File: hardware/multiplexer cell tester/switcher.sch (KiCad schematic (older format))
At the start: 29 parts, among them J3 Conn_01x10_Female, J4 Conn_01x10_Female, J5 A2 Select, J6 A1 Select, J7 A0 Select, U10 ADG839YKSZ-REEL7, U11 ADG839YKSZ-REEL7, U12 ADG839YKSZ-REEL7, U2 CD4518BM96, U2 SN74LVC1G14DRL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

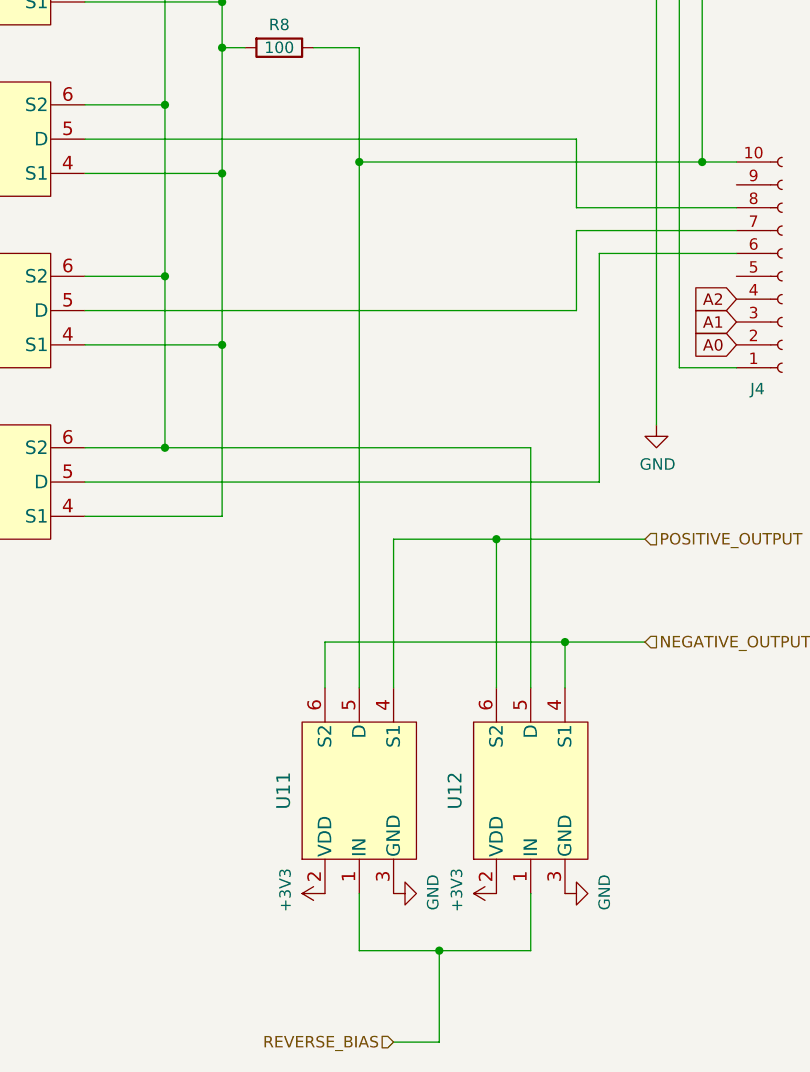
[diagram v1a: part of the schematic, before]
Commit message: Create holders
- Created holders for the payload
- Sliced holders for testing
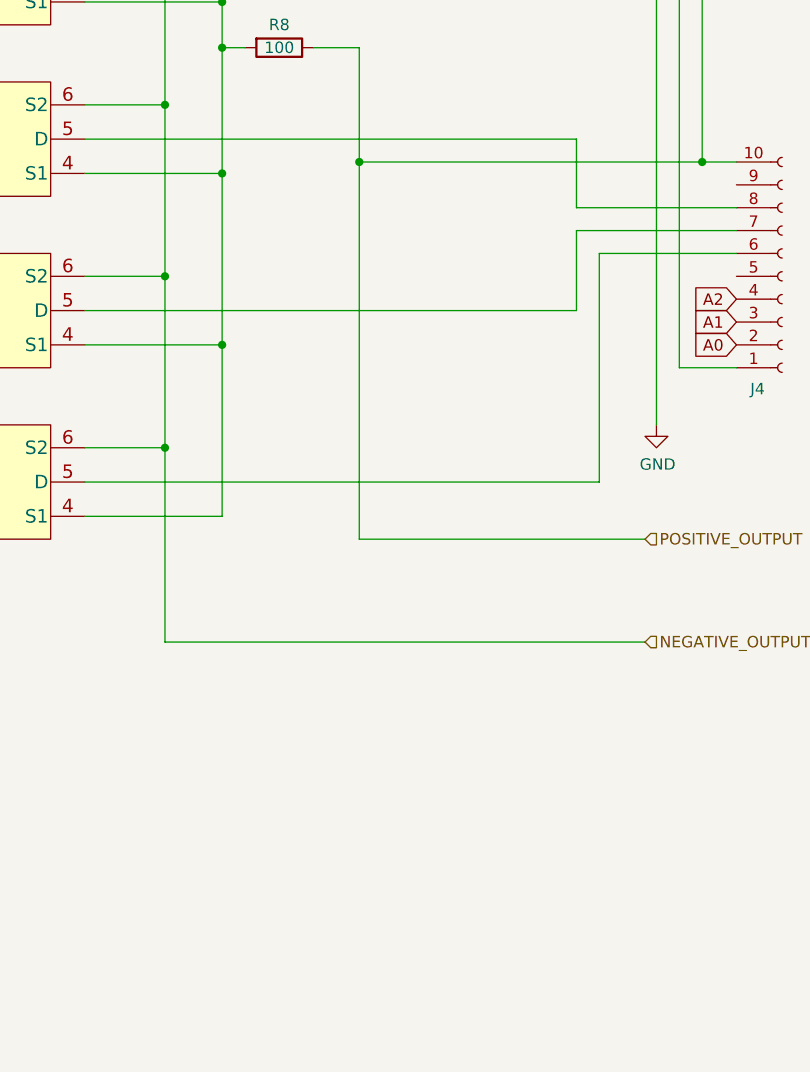
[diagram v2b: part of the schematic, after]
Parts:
- removed U11, U12: ADG839YKSZ-REEL7, ul_ADG839YKSZ-REEL7:ADG839YKSZ-REEL7, symbol ADG839:ADG839YKSZ-REEL7
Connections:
- net NEGATIVE_OUTPUT: now also U10.6 (S2), U5.6 (S2), U6.6 (S2), U7.6 (S2), U8.6 (S2), U9.6 (S2)
- net POSITIVE_OUTPUT: now also J3.1 (Pin_1), J4.10 (Pin_10), R5.1
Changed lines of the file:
@@
 Connection ~ 10050 5750
-Wire Wire Line
-	10050 5750 10050 6500
 Wire Wire Line
 	9700 6500 10050 6500
@@
 Wire Wire Line
 	10700 4750 10900 4750
-$Comp
-L ADG839:ADG839YKSZ-REEL7 U11
-U 1 1 64930E1A
-P 10900 8000
-F 0 "U11" H 10900 8331 60  0000 C CNN
-F 1 "ADG839YKSZ-REEL7" H 10900 8331 60  0001 C CNN
-F 2 "ul_ADG839YKSZ-REEL7:ADG839YKSZ-REEL7" H 10900 8290 60  0001 C CNN
-F 3 "" H 10450 8000 60  0000 C CNN
-	1    10900 8000
-	0    -1   -1   0
-$EndComp
-Wire Wire Line
-	10750 7350 10750 7550
-Wire Wire Line
-	11800 7550 11800 7350
-Wire Wire Line
-	11050 6900 11050 7550
-Wire Wire Line
-	11500 6900 11500 7550
-$Comp
-L power:+3V3 #PWR?
-U 1 1 64B73EC4
-P 10750 8450
-AR Path="/6313FC31/64B73EC4" Ref="#PWR?"  Part="1"
-AR Path="/64B73EC4" Ref="#PWR0210"  Part="1"
-AR Path="/648F7944/64B73EC4" Ref="#PWR0155"  Part="1"
-F 0 "#PWR0155" H 10750 8300 50  0001 C CNN
-F 1 "+3V3" H 10765 8623 50  0000 C CNN
-F 2 "" H 10750 8450 50  0001 C CNN
-F 3 "" H 10750 8450 50  0001 C CNN
-	1    10750 8450
-	0    -1   -1   0
-$EndComp
-$Comp
-L power:+3V3 #PWR?
-U 1 1 64B74C45
-P 11500 8450
-AR Path="/6313FC31/64B74C45" Ref="#PWR?"  Part="1"
-AR Path="/64B74C45" Ref="#PWR0211"  Part="1"
-AR Path="/648F7944/64B74C45" Ref="#PWR0156"  Part="1"
-F 0 "#PWR0156" H 11500 8300 50  0001 C CNN
-F 1 "+3V3" H 11515 8623 50  0000 C CNN
-F 2 "" H 11500 8450 50  0001 C CNN
-F 3 "" H 11500 8450 50  0001 C CNN
-	1    11500 8450
-	0    -1   -1   0
-$EndComp
-$Comp
-L power:GND #PWR?
-U 1 1 64B75863
-P 11050 8450
-AR Path="/6313FC31/64B75863" Ref="#PWR?"  Part="1"
-AR Path="/64B75863" Ref="#PWR0212"  Part="1"
-AR Path="/648F7944/64B75863" Ref="#PWR0157"  Part="1"
-F 0 "#PWR0157" H 11050 8200 50  0001 C CNN
-F 1 "GND" H 11055 8277 50  0000 C CNN
-F 2 "" H 11050 8450 50  0001 C CNN
-F 3 "" H 11050 8450 50  0001 C CNN
-	1    11050 8450
-	0    -1   -1   0
-$EndComp
-$Comp
-L power:GND #PWR?
-U 1 1 64B74F6E
-P 11800 8450
-AR Path="/6313FC31/64B74F6E" Ref="#PWR?"  Part="1"
-AR Path="/64B74F6E" Ref="#PWR0213"  Part="1"
-AR Path="/648F7944/64B74F6E" Ref="#PWR0158"  Part="1"
-F 0 "#PWR0158" H 11800 8200 50  0001 C CNN
-F 1 "GND" H 11805 8277 50  0000 C CNN
-F 2 "" H 11800 8450 50  0001 C CNN
-F 3 "" H 11800 8450 50  0001 C CNN
-	1    11800 8450
-	0    -1   -1   0
-$EndComp
-$Comp
-L ADG839:ADG839YKSZ-REEL7 U12
-U 1 1 6496588F
-P 11650 8000
-F 0 "U12" H 11650 8331 60  0000 C CNN
-F 1 "ADG839YKSZ-REEL7" H 11650 8331 60  0001 C CNN
-F 2 "ul_ADG839YKSZ-REEL7:ADG839YKSZ-REEL7" H 11650 8290 60  0001 C CNN
-F 3 "" H 11200 8000 60  0000 C CNN
-	1    11650 8000
-	0    -1   -1   0
-$EndComp
-Wire Wire Line
-	10750 7350 11800 7350
-Wire Wire Line
-	11050 6900 11500 6900
-Wire Wire Line
-	10900 8450 10900 8700
-Wire Wire Line
-	10900 8700 11250 8700
-Wire Wire Line
-	11650 8700 11650 8450
-Wire Wire Line
-	11250 8700 11250 9100
-Wire Wire Line
-	11250 9100 11050 9100
-Connection ~ 11250 8700
-Wire Wire Line
-	11250 8700 11650 8700
-Wire Wire Line
-	11650 7550 11650 6500
-Wire Wire Line
-	10050 6500 11650 6500
-Wire Wire Line
-	10900 7550 10900 5250
 Wire Wire Line
 	12400 4200 12400 5250
@@
 Text HLabel 12150 7350 2    50   Input ~ 0
 NEGATIVE_OUTPUT
-Wire Wire Line
-	12150 6900 11500 6900
-Connection ~ 11500 6900
-Wire Wire Line
-	11800 7350 12150 7350
-Connection ~ 11800 7350
 $Comp
 L 74xGxx:SN74LVC1G14DRL U2
@@
 Wire Wire Line
 	5700 4550 5800 4550
-Text HLabel 11050 9100 0    50   Input ~ 0
-REVERSE_BIAS
 Text HLabel 12100 4000 0    50   Input ~ 0
 SDA
@@
 	12400 5250 10900 5250
 Connection ~ 12400 5250
+Wire Wire Line
+	10900 5250 10900 4750
+Wire Wire Line
+	10050 5750 10050 6500
+Wire Wire Line
+	10900 6900 10900 5250
+Wire Wire Line
+	10900 6900 12150 6900
 Connection ~ 10900 5250
 Wire Wire Line
-	10900 5250 10900 4750
+	10050 7350 10050 6500
+Wire Wire Line
+	10050 7350 12150 7350
 $EndSCHEMATC

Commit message: Finalized curve tracer
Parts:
- removed C18, C20: 0.1u, Capacitor_SMD:C_0603_1608Metric, symbol Device:C
- added R27, R29, R30, R31, R32: 400, Resistor_SMD:R_0603_1608Metric, symbol Device:R
- R5: value 100 -> 400
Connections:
- net POSITIVE_OUTPUT: now also R27.1, R29.1, R30.1, R31.1, R32.1
- new net: R32.2, U10.4 (S1)
- new net: R5.2, U7.4 (S1)
- new net: R30.2, U8.4 (S1)
- new net: R29.2, U6.4 (S1)
- new net: R31.2, U9.4 (S1)
- new net: R27.2, U5.4 (S1)
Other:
- moved on the sheet: C13, R8
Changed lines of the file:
@@
 Sheet 2 4
 Title "Perovskite Switching Circuit"
-Date "2023-07-08"
+Date "2023-09-08"
 Rev "B"
 Comp "Aerospace eXperimental Payloads | UNL Aerospace Club"
@@
 $EndComp
 $Comp
-L Device:C C?
-U 1 1 63AAB0E4
-P 3800 1250
-AR Path="/6313FC31/63AAB0E4" Ref="C?"  Part="1"
-AR Path="/63AAB0E4" Ref="C20"  Part="1"
-AR Path="/648F7944/63AAB0E4" Ref="C8"  Part="1"
-F 0 "C8" V 4052 1250 50  0000 C CNN
-F 1 "0.1u" V 3961 1250 50  0000 C CNN
-F 2 "Capacitor_SMD:C_0603_1608Metric" H 3838 1100 50  0001 C CNN
-F 3 "~" H 3800 1250 50  0001 C CNN
-	1    3800 1250
-	1    0    0    -1
-$EndComp
-$Comp
-L power:+3V3 #PWR?
-U 1 1 63AAB0EA
-P 3800 1100
-AR Path="/6313FC31/63AAB0EA" Ref="#PWR?"  Part="1"
-AR Path="/63AAB0EA" Ref="#PWR0172"  Part="1"
-AR Path="/648F7944/63AAB0EA" Ref="#PWR0131"  Part="1"
-F 0 "#PWR0131" H 3800 950 50  0001 C CNN
-F 1 "+3V3" H 3815 1273 50  0000 C CNN
-F 2 "" H 3800 1100 50  0001 C CNN
-F 3 "" H 3800 1100 50  0001 C CNN
-	1    3800 1100
-	1    0    0    -1
-$EndComp
-$Comp
-L power:GND #PWR?
-U 1 1 63AAB0F0
-P 3800 1400
-AR Path="/6313FC31/63AAB0F0" Ref="#PWR?"  Part="1"
-AR Path="/63AAB0F0" Ref="#PWR0173"  Part="1"
-AR Path="/648F7944/63AAB0F0" Ref="#PWR0132"  Part="1"
-F 0 "#PWR0132" H 3800 1150 50  0001 C CNN
-F 1 "GND" H 3805 1227 50  0000 C CNN
-F 2 "" H 3800 1400 50  0001 C CNN
-F 3 "" H 3800 1400 50  0001 C CNN
-	1    3800 1400
-	1    0    0    -1
-$EndComp
-$Comp
-L Device:C C?
-U 1 1 63AAB0F6
-P 3400 1250
-AR Path="/6313FC31/63AAB0F6" Ref="C?"  Part="1"
-AR Path="/63AAB0F6" Ref="C18"  Part="1"
-AR Path="/648F7944/63AAB0F6" Ref="C7"  Part="1"
-F 0 "C7" V 3652 1250 50  0000 C CNN
-F 1 "0.1u" V 3561 1250 50  0000 C CNN
-F 2 "Capacitor_SMD:C_0603_1608Metric" H 3438 1100 50  0001 C CNN
-F 3 "~" H 3400 1250 50  0001 C CNN
-	1    3400 1250
-	1    0    0    -1
-$EndComp
-$Comp
-L power:+3V3 #PWR?
-U 1 1 63AAB0FC
-P 3400 1100
-AR Path="/6313FC31/63AAB0FC" Ref="#PWR?"  Part="1"
-AR Path="/63AAB0FC" Ref="#PWR0174"  Part="1"
-AR Path="/648F7944/63AAB0FC" Ref="#PWR0133"  Part="1"
-F 0 "#PWR0133" H 3400 950 50  0001 C CNN
-F 1 "+3V3" H 3415 1273 50  0000 C CNN
-F 2 "" H 3400 1100 50  0001 C CNN
-F 3 "" H 3400 1100 50  0001 C CNN
-	1    3400 1100
-	1    0    0    -1
-$EndComp
-$Comp
-L power:GND #PWR?
-U 1 1 63AAB102
-P 3400 1400
-AR Path="/6313FC31/63AAB102" Ref="#PWR?"  Part="1"
-AR Path="/63AAB102" Ref="#PWR0175"  Part="1"
-AR Path="/648F7944/63AAB102" Ref="#PWR0134"  Part="1"
-F 0 "#PWR0134" H 3400 1150 50  0001 C CNN
-F 1 "GND" H 3405 1227 50  0000 C CNN
-F 2 "" H 3400 1400 50  0001 C CNN
-F 3 "" H 3400 1400 50  0001 C CNN
-	1    3400 1400
-	1    0    0    -1
-$EndComp
-$Comp
 L ADG839:ADG839YKSZ-REEL7 U10
 U 1 1 63F8A2FD
@@
 Wire Wire Line
 	10050 2750 10050 3500
-Wire Wire Line
-	10300 3050 9700 3050
 $Comp
 L Device:R R?
 U 1 1 6435678E
-P 10550 4750
+P 10550 4550
 AR Path="/6313FC31/6435678E" Ref="R?"  Part="1"
 AR Path="/6435678E" Ref="R5"  Part="1"
 AR Path="/648F7944/6435678E" Ref="R8"  Part="1"
-F 0 "R8" V 10450 4750 50  0000 C CNN
-F 1 "100" V 10550 4750 50  0000 C CNN
-F 2 "Resistor_SMD:R_0603_1608Metric" V 10480 4750 50  0001 C CNN
-F 3 "~" H 10550 4750 50  0001 C CNN
-	1    10550 4750
+F 0 "R8" V 10450 4550 50  0000 C CNN
+F 1 "400" V 10550 4550 50  0000 C CNN
+F 2 "Resistor_SMD:R_0603_1608Metric" V 10480 4550 50  0001 C CNN
+F 3 "~" H 10550 4550 50  0001 C CNN
+	1    10550 4550
 	0    1    1    0
 $EndComp
@@
 Wire Wire Line
 	9700 6500 10050 6500
-Wire Wire Line
-	10300 3050 10300 3800
-Wire Wire Line
-	9700 6800 10300 6800
-Wire Wire Line
-	9700 6050 10300 6050
-Connection ~ 10300 6050
-Wire Wire Line
-	9700 5300 10300 5300
-Connection ~ 10300 5300
-Wire Wire Line
-	10300 5300 10300 6050
-Wire Wire Line
-	9700 4550 10300 4550
-Connection ~ 10300 4550
-Wire Wire Line
-	9700 3800 10300 3800
-Connection ~ 10300 3800
-Wire Wire Line
-	10300 3800 10300 4550
-Wire Wire Line
-	10300 6050 10300 6800
 $Comp
 L ADG839:ADG839YKSZ-REEL7 U9
@@
 L Device:C C?
 U 1 1 64C38237
-P 5000 1250
+P 4650 1250
 AR Path="/6313FC31/64C38237" Ref="C?"  Part="1"
 AR Path="/64C38237" Ref="C25"  Part="1"
 AR Path="/648F7944/64C38237" Ref="C13"  Part="1"
-F 0 "C13" V 5252 1250 50  0000 C CNN
-F 1 "0.1u" V 5161 1250 50  0000 C CNN
-F 2 "Capacitor_SMD:C_0603_1608Metric" H 5038 1100 50  0001 C CNN
-F 3 "~" H 5000 1250 50  0001 C CNN
-	1    5000 1250
+F 0 "C13" V 4902 1250 50  0000 C CNN
+F 1 "0.1u" V 4811 1250 50  0000 C CNN
+F 2 "Capacitor_SMD:C_0603_1608Metric" H 4688 1100 50  0001 C CNN
+F 3 "~" H 4650 1250 50  0001 C CNN
+	1    4650 1250
 	1    0    0    -1
 $EndComp
@@
 L power:+3V3 #PWR?
 U 1 1 64C3823D
-P 5000 1100
+P 4650 1100
 AR Path="/6313FC31/64C3823D" Ref="#PWR?"  Part="1"
 AR Path="/64C3823D" Ref="#PWR0214"  Part="1"
 AR Path="/648F7944/64C3823D" Ref="#PWR0149"  Part="1"
-F 0 "#PWR0149" H 5000 950 50  0001 C CNN
-F 1 "+3V3" H 5015 1273 50  0000 C CNN
-F 2 "" H 5000 1100 50  0001 C CNN
-F 3 "" H 5000 1100 50  0001 C CNN
-	1    5000 1100
+F 0 "#PWR0149" H 4650 950 50  0001 C CNN
+F 1 "+3V3" H 4665 1273 50  0000 C CNN
+F 2 "" H 4650 1100 50  0001 C CNN
+F 3 "" H 4650 1100 50  0001 C CNN
+	1    4650 1100
 	1    0    0    -1
 $EndComp
@@
 L power:GND #PWR?
 U 1 1 64C38243
-P 5000 1400
+P 4650 1400
 AR Path="/6313FC31/64C38243" Ref="#PWR?"  Part="1"
 AR Path="/64C38243" Ref="#PWR0215"  Part="1"
 AR Path="/648F7944/64C38243" Ref="#PWR0150"  Part="1"
-F 0 "#PWR0150" H 5000 1150 50  0001 C CNN
-F 1 "GND" H 5005 1227 50  0000 C CNN
-F 2 "" H 5000 1400 50  0001 C CNN
-F 3 "" H 5000 1400 50  0001 C CNN
-	1    5000 1400
+F 0 "#PWR0150" H 4650 1150 50  0001 C CNN
+F 1 "GND" H 4655 1227 50  0000 C CNN
+F 2 "" H 4650 1400 50  0001 C CNN
+F 3 "" H 4650 1400 50  0001 C CNN
+	1    4650 1400
 	1    0    0    -1
 $EndComp
@@
 Connection ~ 10050 6500
 Wire Wire Line
-	10300 4550 10300 4750
-Wire Wire Line
-	10400 4750 10300 4750
-Connection ~ 10300 4750
-Wire Wire Line
-	10300 4750 10300 5300
-Wire Wire Line
 	12100 3900 12550 3900
 Wire Wire Line
@@
 	15300 7200 15300 7350
 Wire Wire Line
-	10700 4750 10900 4750
-Wire Wire Line
 	12400 4200 12400 5250
 Wire Wire Line
@@
 Connection ~ 12400 5250
 Wire Wire Line
-	10900 5250 10900 4750
-Wire Wire Line
 	10050 5750 10050 6500
 Wire Wire Line
-	10900 6900 10900 5250
+	10900 6900 10900 6800
 Wire Wire Line
 	10900 6900 12150 6900
@@
 Wire Wire Line
 	10050 7350 12150 7350
+Wire Wire Line
+	9700 4550 10400 4550
+Wire Wire Line
+	10700 4550 10900 4550
+Wire Wire Line
+	10900 4550 10900 5250
+$Comp
+L Device:R R?
+U 1 1 6503BEC1
+P 10550 5300
+AR Path="/6313FC31/6503BEC1" Ref="R?"  Part="1"
+AR Path="/6503BEC1" Ref="R?"  Part="1"
+AR Path="/648F7944/6503BEC1" Ref="R30"  Part="1"
+F 0 "R30" V 10450 5300 50  0000 C CNN
+F 1 "400" V 10550 5300 50  0000 C CNN
+F 2 "Resistor_SMD:R_0603_1608Metric" V 10480 5300 50  0001 C CNN
+F 3 "~" H 10550 5300 50  0001 C CNN
+	1    10550 5300
+	0    1    1    0
+$EndComp
+$Comp
+L Device:R R?
+U 1 1 6503C07C
+P 10550 6050
+AR Path="/6313FC31/6503C07C" Ref="R?"  Part="1"
+AR Path="/6503C07C" Ref="R?"  Part="1"
+AR Path="/648F7944/6503C07C" Ref="R31"  Part="1"
+F 0 "R31" V 10450 6050 50  0000 C CNN
+F 1 "400" V 10550 6050 50  0000 C CNN
+F 2 "Resistor_SMD:R_0603_1608Metric" V 10480 6050 50  0001 C CNN
+F 3 "~" H 10550 6050 50  0001 C CNN
+	1    10550 6050
+	0    1    1    0
+$EndComp
+$Comp
+L Device:R R?
+U 1 1 6503C237
+P 10550 6800
+AR Path="/6313FC31/6503C237" Ref="R?"  Part="1"
+AR Path="/6503C237" Ref="R?"  Part="1"
+AR Path="/648F7944/6503C237" Ref="R32"  Part="1"
+F 0 "R32" V 10450 6800 50  0000 C CNN
+F 1 "400" V 10550 6800 50  0000 C CNN
+F 2 "Resistor_SMD:R_0603_1608Metric" V 10480 6800 50  0001 C CNN
+F 3 "~" H 10550 6800 50  0001 C CNN
+	1    10550 6800
+	0    1    1    0
+$EndComp
+$Comp
+L Device:R R?
+U 1 1 6503C3F2
+P 10550 3800
+AR Path="/6313FC31/6503C3F2" Ref="R?"  Part="1"
+AR Path="/6503C3F2" Ref="R?"  Part="1"
+AR Path="/648F7944/6503C3F2" Ref="R29"  Part="1"
+F 0 "R29" V 10450 3800 50  0000 C CNN
+F 1 "400" V 10550 3800 50  0000 C CNN
+F 2 "Resistor_SMD:R_0603_1608Metric" V 10480 3800 50  0001 C CNN
+F 3 "~" H 10550 3800 50  0001 C CNN
+	1    10550 3800
+	0    1    1    0
+$EndComp
+$Comp
+L Device:R R?
+U 1 1 6503C606
+P 10550 3050
+AR Path="/6313FC31/6503C606" Ref="R?"  Part="1"
+AR Path="/6503C606" Ref="R?"  Part="1"
+AR Path="/648F7944/6503C606" Ref="R27"  Part="1"
+F 0 "R27" V 10450 3050 50  0000 C CNN
+F 1 "400" V 10550 3050 50  0000 C CNN
+F 2 "Resistor_SMD:R_0603_1608Metric" V 10480 3050 50  0001 C CNN
+F 3 "~" H 10550 3050 50  0001 C CNN
+	1    10550 3050
+	0    1    1    0
+$EndComp
+Wire Wire Line
+	10700 3050 10900 3050
+Wire Wire Line
+	10900 3050 10900 3800
+Connection ~ 10900 4550
+Wire Wire Line
+	9700 3050 10400 3050
+Wire Wire Line
+	9700 3800 10400 3800
+Wire Wire Line
+	9700 5300 10400 5300
+Wire Wire Line
+	9700 6050 10400 6050
+Wire Wire Line
+	9700 6800 10400 6800
+Wire Wire Line
+	10700 6800 10900 6800
+Connection ~ 10900 6800
+Wire Wire Line
+	10900 6800 10900 6050
+Wire Wire Line
+	10700 6050 10900 6050
+Connection ~ 10900 6050
+Wire Wire Line
+	10900 6050 10900 5300
+Wire Wire Line
+	10700 5300 10900 5300
+Connection ~ 10900 5300
+Wire Wire Line
+	10900 5300 10900 5250
+Wire Wire Line
+	10700 3800 10900 3800
+Connection ~ 10900 3800
+Wire Wire Line
+	10900 3800 10900 4550
 $EndSCHEMATC
